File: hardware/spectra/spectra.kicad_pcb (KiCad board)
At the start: 2 copper layers, 40 x 18 mm, 0 parts

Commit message: Fully routed
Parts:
- added C1: 4.5uF, Capacitor_SMD:C_0603_1608Metric, F.Cu at (131.5, 102.5)
- added C2: 0.1uF, Capacitor_SMD:C_0402_1005Metric, F.Cu at (133.5, 104.5)
- added C3: 10uF, Capacitor_SMD:C_0603_1608Metric, F.Cu at (133.5, 111.5)
- added D1: CUS551V30,H3F, Diode_SMD:D_SOD-323, F.Cu at (128.5, 101.5)
- added H1: MountingHole, cycfi_library:mounting_hole_2.1mm, F.Cu at (103.0, 103.0)
- added H2: MountingHole, cycfi_library:mounting_hole_2.1mm, F.Cu at (103.0, 115.0)
- added H3: MountingHole, cycfi_library:mounting_hole_2.1mm, F.Cu at (137.0, 103.0)
- added H4: MountingHole, cycfi_library:mounting_hole_2.1mm, F.Cu at (137.0, 115.0)
- added J1: I/O, cycfi_library:pin_header_2x5p_2.54mm_smd_horizontal, F.Cu at (110.0, 109.0)
- added J4: Coil, cycfi_library:pin_socket_2x3p_1.00mm_smd_vertical, B.Cu at (104.8, 109.0)
- added R1: 39k, Resistor_SMD:R_0402_1005Metric, F.Cu at (132.0, 106.5)
- added R2: 39k, Resistor_SMD:R_0402_1005Metric, F.Cu at (136.5, 110.0)
- added R3: 300k, Resistor_SMD:R_0402_1005Metric, F.Cu at (138.0, 107.5)
- added R4: 300k, Resistor_SMD:R_0402_1005Metric, F.Cu at (132.5, 109.0)
- added R5: 150k, Resistor_SMD:R_0402_1005Metric, F.Cu at (136.5, 111.5)
- added R6: 10k, Resistor_SMD:R_0402_1005Metric, F.Cu at (130.5, 109.0)
- added R7: 4.7k, Resistor_SMD:R_0402_1005Metric, F.Cu at (130.5, 111.5)
- added U1: TLV170DBV, Package_TO_SOT_SMD:SOT-23-5, F.Cu at (135.5, 107.5)
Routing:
- net ext_coil_1: track 0.00 -> 43.3 mm
- net Net-(J4-Pad6): track 0.00 -> 35.9 mm, vias 0 -> 1
- net GND: track 0.00 -> 33.2 mm, vias 0 -> 4
- net Out: track 0.00 -> 27.9 mm
- net mix_shunt_1: track 0.00 -> 24.0 mm
- net Net-(D1-Pad2): track 0.00 -> 17.3 mm
- net V+: track 0.00 -> 11.6 mm
- net Net-(R1-Pad1): track 0.00 -> 9.53 mm
- net ext_coil_2: track 0.00 -> 9.17 mm, vias 0 -> 1
- net Net-(C3-Pad2): track 0.00 -> 8.91 mm, vias 0 -> 2
- net Net-(R2-Pad2): track 0.00 -> 3.22 mm
- net Net-(J4-Pad3): track 0.00 -> 3.20 mm
- added copper zone on B.Cu, net GND
- added copper zone on F.Cu, net GND
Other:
- outline, holes or cut-outs redrawn

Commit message: added logo
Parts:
- added G***: LOGO, cycfi_library:cycfi-logo-15mm, F.Cu at (126.6, 116.3)
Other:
- board text added: "Spectra Preamp v1.0"

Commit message: Merge branch 'reversed' into master
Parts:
- H1, H2, H3, H4: moved to B.Cu
- moved J4 32.2 mm to (137.0, 109.0), turned to 90 degrees
- moved R5 27.5 mm to (109.0, 110.0)
- moved U1 27.5 mm to (108.0, 107.0)
- moved C2 27.1 mm to (106.5, 102.5), turned to 270 degrees
- moved R3 26.5 mm to (111.5, 106.0), turned to 0 degrees
- moved C3 26.5 mm to (107.0, 111.0), turned to 90 degrees
- moved R2 25.0 mm to (111.5, 109.0), turned to 180 degrees
- moved C1 23.0 mm to (108.5, 103.0)
- moved R6 21.6 mm to (109.0, 111.5), turned to 0 degrees
- moved R7 21.6 mm to (109.0, 113.0), turned to 180 degrees
- moved R4 21.1 mm to (111.5, 107.5), turned to 0 degrees
- moved R1 20.6 mm to (111.5, 104.5)
- moved J1 20.0 mm to (130.0, 109.0), turned to 180 degrees
- moved D1 17.0 mm to (111.5, 102.5), turned to 0 degrees
- moved G*** 13.6 mm to (113.0, 116.4), turned to 0 degrees
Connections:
- net ext_coil_1 renamed ext_coil+
- C3 pad 1: mix_shunt_1 -> out
- D1 pad 2: Net-(D1-Pad2) -> /VCC
- J1 pad 10: Net-(D1-Pad2) -> out
- J1 pad 2: GND -> ext_coil-
- J1 pad 3: ext_coil_2 -> ext_coil-
- J1 pad 4: ext_coil_2 -> GND
- J1 pad 6: Out -> /VCC
- J1 pad 7: mix_shunt_1 -> GND
- J1 pad 8: Out -> mix
- J1 pad 9: GND -> mix
- J4 pad 1: ext_coil_2 -> ext_coil-
- J4 pad 3: Net-(J4-Pad3) -> /IN-
- J4 pad 4: Net-(J4-Pad3) -> /IN-
- J4 pad 6: Net-(J4-Pad6) -> ext_coil-
- R2 pad 1: Net-(J4-Pad6) -> /IN-
- R6 pad 1: mix_shunt_1 -> out
- R7 pad 1: Out -> mix
- R7 pad 2: mix_shunt_1 -> out
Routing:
- net Net-(J4-Pad6): track 35.9 -> 0.00 mm, vias 1 -> 0
- net Out: track 27.9 -> 0.00 mm
- net /IN-: track 0.00 -> 27.9 mm, vias 0 -> 1
- net out: track 0.00 -> 27.4 mm
- net mix: track 0.00 -> 25.6 mm
- net mix_shunt_1: track 24.0 -> 0.00 mm
- net Net-(D1-Pad2): track 17.3 -> 0.00 mm
- net GND: track 33.2 -> 49.5 mm, vias 4 -> 3
- net /VCC: track 0.00 -> 16.0 mm
- net ext_coil-: track 0.00 -> 15.3 mm, vias 0 -> 1
- net ext_coil_2: track 9.17 -> 0.00 mm, vias 1 -> 0
- net Net-(J4-Pad3): track 3.20 -> 0.00 mm
- net V+: track 11.6 -> 10.1 mm
- net Net-(R2-Pad2): track 3.22 -> 4.62 mm
- net ext_coil+: track 43.3 -> 41.9 mm
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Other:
- board text added: "Spectra Active v1.0"
- board text removed: "Spectra Preamp v1.0"

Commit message: added 3d model for 2x5 pin header
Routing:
- net GND: track 49.5 -> 33.3 mm, vias 3 -> 2
- net mix: track 25.6 -> 22.2 mm
- net ext_coil+: track 41.9 -> 44.8 mm
- net out: track 27.4 -> 25.1 mm
- net ext_coil-: track 15.3 -> 13.9 mm

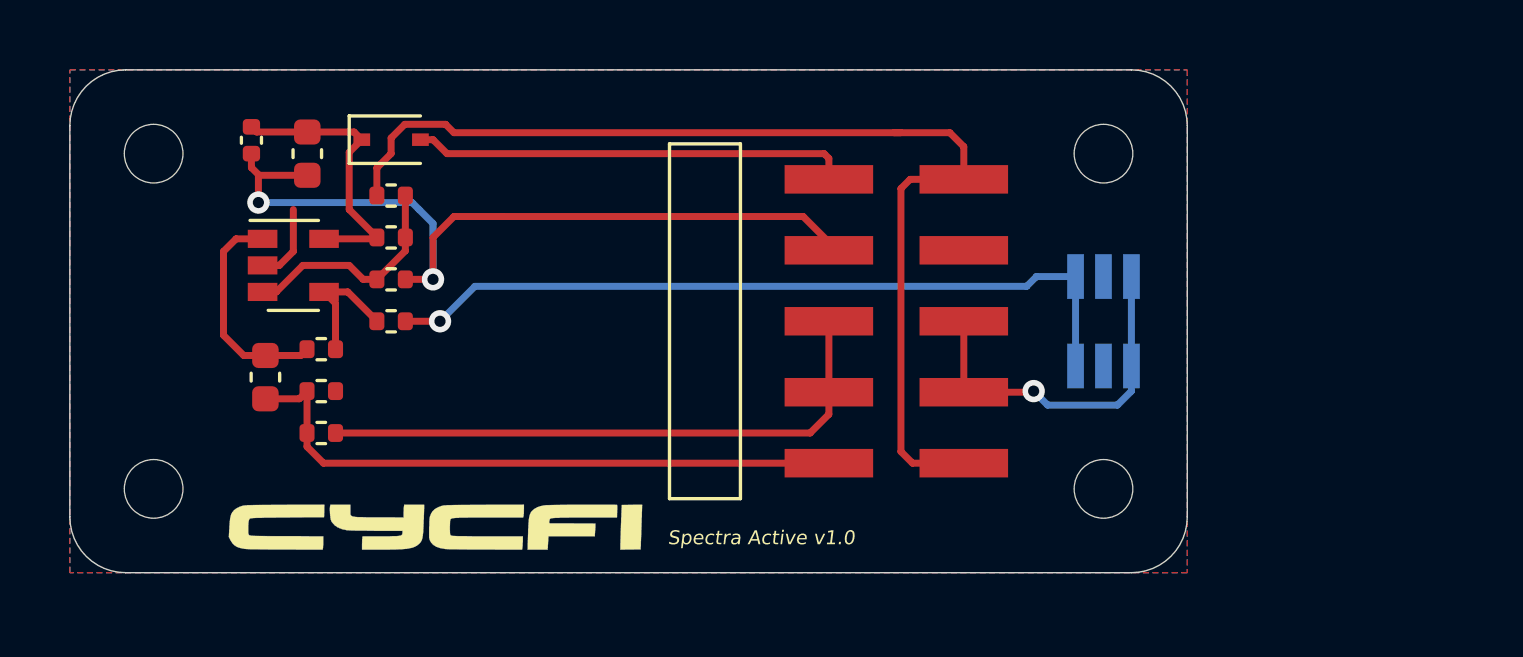
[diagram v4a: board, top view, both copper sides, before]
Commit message: - Increased PCB length to 50mm - Added legend
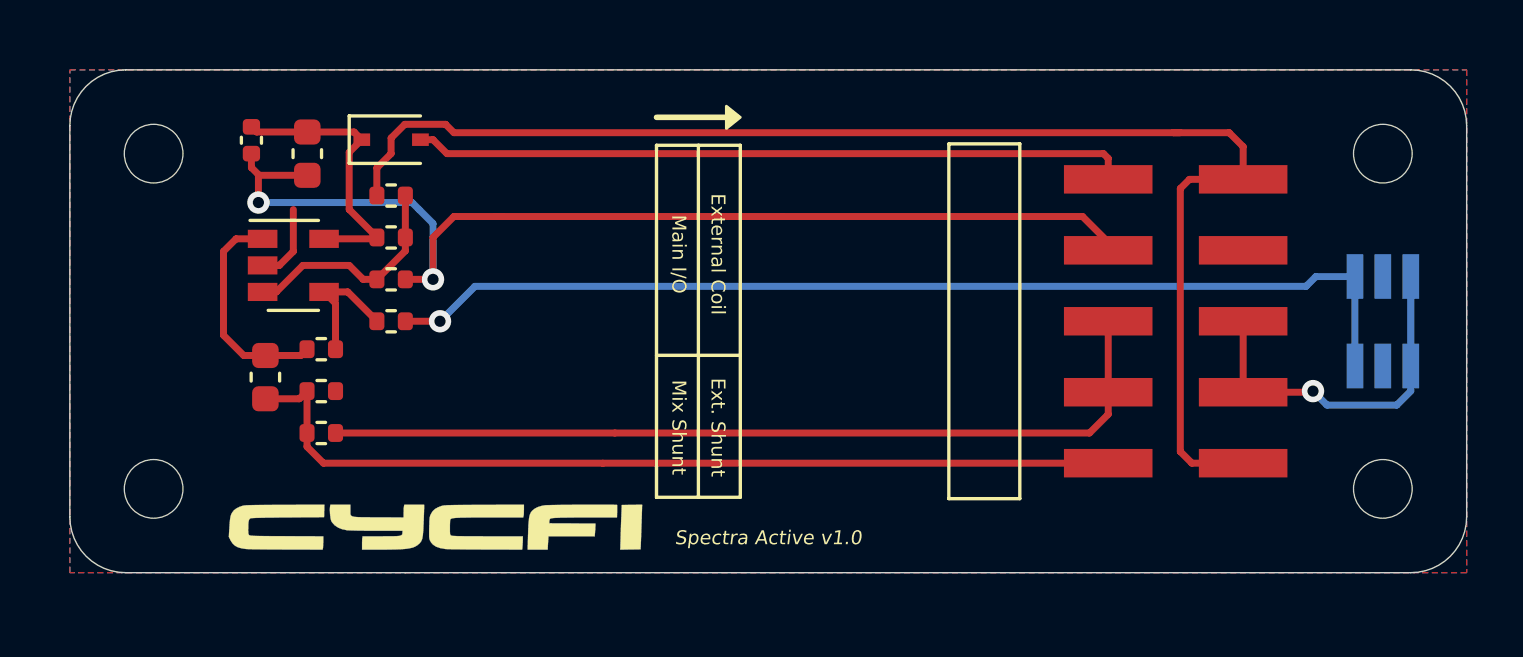
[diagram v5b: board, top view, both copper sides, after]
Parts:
- moved H3 10.0 mm to (147.0, 103.0)
- moved H4 10.0 mm to (147.0, 115.0)
- moved J1 10.0 mm to (140.0, 109.0)
- moved J4 10.0 mm to (147.0, 109.0)
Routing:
- net GND: track 33.3 -> 43.5 mm
- net /IN-: track 27.9 -> 37.9 mm
- net ext_coil+: track 44.8 -> 54.8 mm
- net mix: track 22.2 -> 32.2 mm
- net /VCC: track 15.6 -> 25.6 mm
- net out: track 25.1 -> 35.1 mm
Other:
- board size 40 x 18 mm -> 50 x 18 mm
- board text added: "Ext. Shunt"
- board text added: "External Coil"
- board text added: "Main I/O"
- board text added: "Mix Shunt"

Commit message: Nu name
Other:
- board text added: "Nu Spectra Preamp v1.0"
- board text removed: "Spectra Active v1.0"

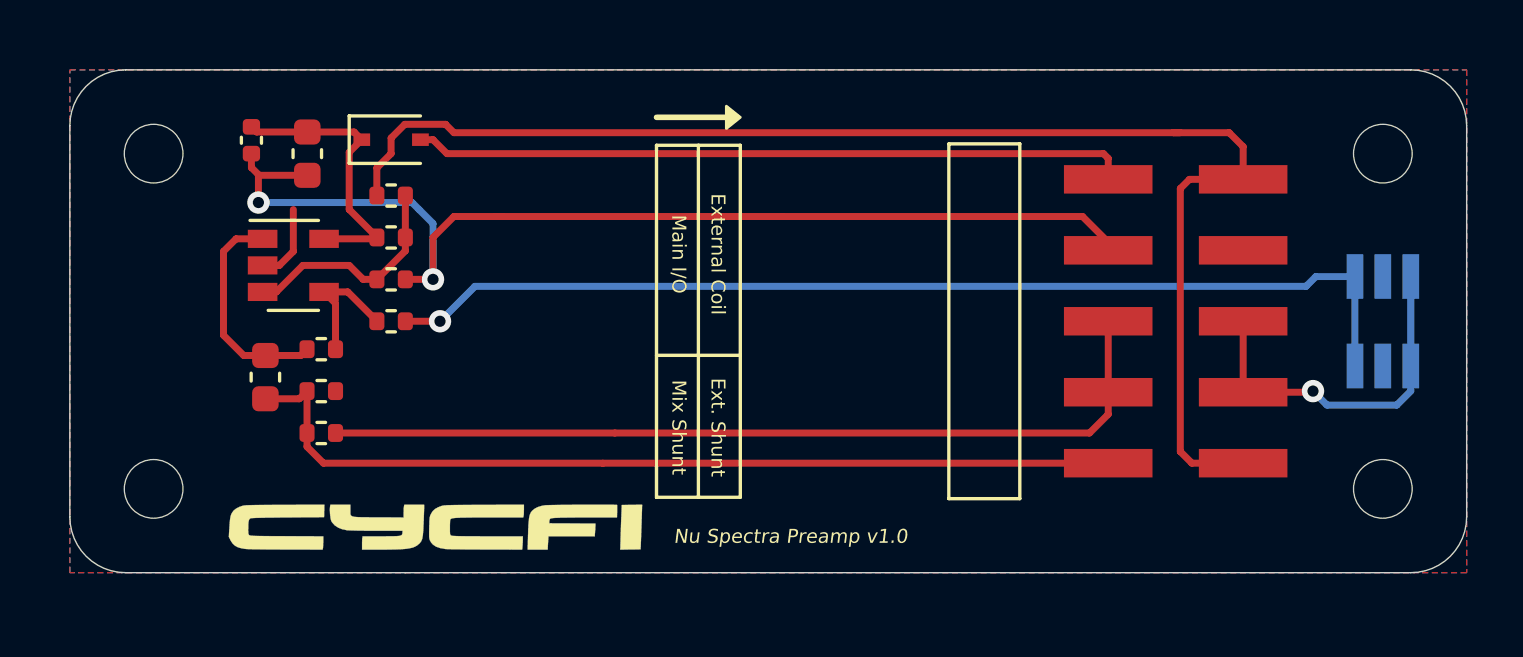
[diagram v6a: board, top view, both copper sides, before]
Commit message: Smaller board
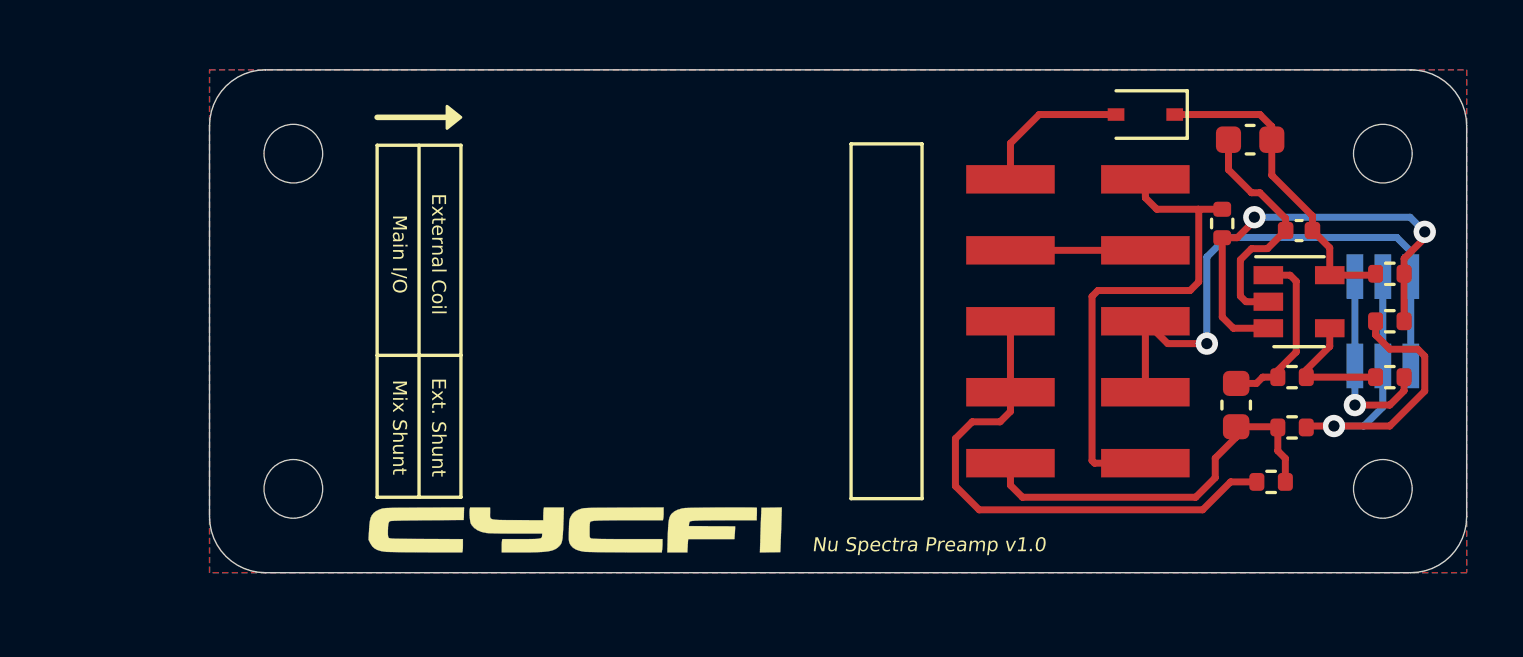
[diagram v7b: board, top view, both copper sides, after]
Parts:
- moved C2 37.6 mm to (144.0, 105.8), turned to 180 degrees
- moved U1 36.0 mm to (144.0, 108.3)
- moved R2 35.8 mm to (147.2, 111.0)
- moved R4 35.8 mm to (147.2, 109.0), turned to 180 degrees
- moved R3 35.8 mm to (147.2, 107.3)
- moved R6 34.8 mm to (143.8, 112.8)
- moved C3 34.8 mm to (141.8, 112.0)
- moved R5 34.8 mm to (143.8, 111.0)
- moved R7 34.0 mm to (143.0, 114.8), turned to 0 degrees
- moved C1 33.8 mm to (142.2, 102.5), turned to 180 degrees
- moved R1 29.8 mm to (141.2, 105.5), turned to 90 degrees
- moved D1 27.0 mm to (138.5, 101.6), turned to 180 degrees
- moved G*** 5.00 mm to (118.0, 116.5)
- moved H1 5.00 mm to (108.0, 103.0)
- moved H2 5.00 mm to (108.0, 115.0)
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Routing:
- net ext_coil+: track 54.8 -> 18.1 mm
- net /IN-: track 37.9 -> 7.06 mm
- net out: track 35.1 -> 14.3 mm
- net /VCC: track 25.6 -> 5.50 mm
- net GND: track 43.5 -> 28.8 mm, vias 2 -> 1
- net mix: track 32.2 -> 18.9 mm
- net Net-(R1-Pad1): track 8.17 -> 16.0 mm, vias 0 -> 2
- net ext_coil-: track 13.9 -> 20.1 mm
- net Net-(C3-Pad2): track 7.97 -> 6.38 mm
- net V+: track 10.1 -> 11.5 mm
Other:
- board size 50 x 18 mm -> 45 x 18 mm

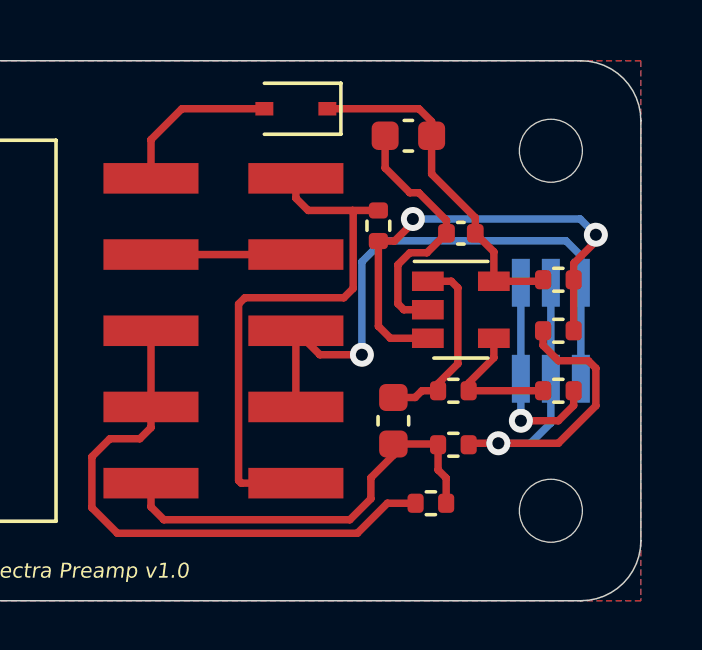
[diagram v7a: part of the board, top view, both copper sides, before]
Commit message: improve the layout
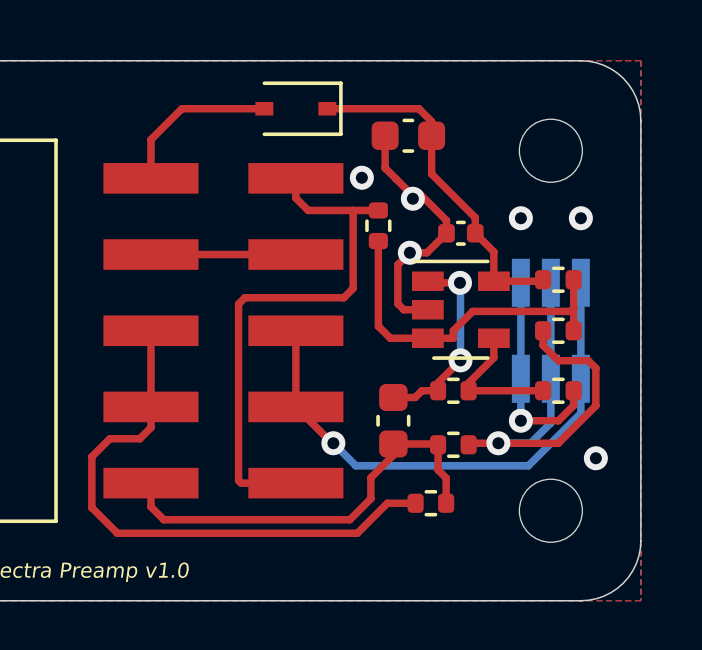
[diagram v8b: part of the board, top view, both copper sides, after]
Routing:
- net Net-(R1-Pad1): track 16.0 -> 11.8 mm, vias 2 -> 0
- net ext_coil-: track 20.1 -> 18.3 mm
- net Net-(C3-Pad2): track 6.38 -> 6.83 mm, vias 0 -> 2
- net GND: vias 1 -> 7
